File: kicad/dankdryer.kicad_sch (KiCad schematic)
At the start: 23 parts, among them J1 Barreljack, J4 heater, J6 Screw_Terminal_01x05, J7 5kg load cell, J8 motor, J9 Conn_01x04, U2 TPS62162DSG, U3 HT7550, U6 ESP32-C6-MINI-1U

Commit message: add 0.1uf capacitor to ADC input line closes #78
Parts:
- added C14: 0.1u, Capacitor_SMD:C_0805_2012Metric_Pad1.18x1.45mm_HandSolder, symbol Device:C
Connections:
- net GND: now also C14.1
- net Therm: now also C14.2
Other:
- note added: "ESP32 pins tolerate 20mA@3.3V. 412Ω+680Ω takes 5.3V to 3.369V and 5V to 3.178V, and limits current to 12.1mA. ESP32 ADC wants a 0.1uF filter capacitor "to improve accuracy"."
- note removed: "ESP32 pins tolerate 20mA@3.3V. 412Ω+680Ω takes 5.3V to 3.369V and 5V to 3.178V, and limits current to 12.1mA."
- moved on the sheet: R16, R18
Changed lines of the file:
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@@
 	)
 	(junction
+		(at 187.96 64.77)
+		(diameter 0)
+		(color 0 0 0 0)
+	)
+	(junction
 		(at 52.07 43.18)
 		(diameter 0)
@@
 	)
 	(junction
-		(at 71.12 147.32)
+		(at 66.04 147.32)
 		(diameter 0)
 		(color 0 0 0 0)
@@
 	)
 	(junction
+		(at 72.39 147.32)
+		(diameter 0)
+		(color 0 0 0 0)
+	)
+	(junction
 		(at 97.79 83.82)
 		(diameter 0)
@@
 	(wire
 		(pts
-			(xy 82.55 154.94) (xy 82.55 133.35)
+			(xy 82.55 137.16) (xy 82.55 133.35)
 		)
 		(stroke
@@
 	(wire
 		(pts
-			(xy 71.12 139.7) (xy 71.12 135.89)
+			(xy 66.04 139.7) (xy 66.04 135.89)
 		)
 		(stroke
@@
 	(wire
 		(pts
-			(xy 58.42 135.89) (xy 71.12 135.89)
+			(xy 58.42 135.89) (xy 66.04 135.89)
 		)
 		(stroke
@@
 	(wire
 		(pts
-			(xy 73.66 147.32) (xy 71.12 147.32)
+			(xy 74.93 147.32) (xy 72.39 147.32)
 		)
 		(stroke
@@
 	(wire
 		(pts
+			(xy 187.96 64.77) (xy 189.23 64.77)
+		)
+		(stroke
+			(width 0)
+			(type default)
+		)
+	)
+	(wire
+		(pts
 			(xy 132.08 185.42) (xy 127 185.42)
 		)
@@
 	(wire
 		(pts
+			(xy 72.39 147.32) (xy 66.04 147.32)
+		)
+		(stroke
+			(width 0)
+			(type default)
+		)
+	)
+	(wire
+		(pts
 			(xy 34.29 189.23) (xy 36.83 189.23)
 		)
@@
 	(wire
 		(pts
+			(xy 185.42 64.77) (xy 187.96 64.77)
+		)
+		(stroke
+			(width 0)
+			(type default)
+		)
+	)
+	(wire
+		(pts
 			(xy 219.71 85.09) (xy 223.52 85.09)
 		)
@@
 	(wire
 		(pts
+			(xy 187.96 68.58) (xy 187.96 64.77)
+		)
+		(stroke
+			(width 0)
+			(type default)
+		)
+	)
+	(wire
+		(pts
 			(xy 67.31 186.69) (xy 63.5 186.69)
 		)
@@
 		)
 	)
-	(text "ESP32 pins tolerate 20mA@3.3V.\n412Ω+680Ω takes 5.3V to 3.369V and 5V to 3.178V,\n and limits current to 12.1mA."
+	(text "ESP32 pins tolerate 20mA@3.3V.\n412Ω+680Ω takes 5.3V to 3.369V and 5V to 3.178V,\n and limits current to 12.1mA.\nESP32 ADC wants a 0.1uF filter capacitor \"to improve accuracy\"."
 		(exclude_from_sim no)
-		(at 21.336 164.084 0)
+		(at 21.082 163.576 0)
 		(effects
 			(font
@@
 	(hierarchical_label "Therm"
 		(shape bidirectional)
-		(at 189.23 64.77 180)
+		(at 185.42 64.77 180)
 		(fields_autoplaced yes)
 		(effects
@@
 	(hierarchical_label "Therm"
 		(shape input)
-		(at 73.66 147.32 0)
+		(at 74.93 147.32 0)
 		(fields_autoplaced yes)
 		(effects
@@
 	(symbol
 		(lib_id "Device:R")
-		(at 71.12 143.51 0)
+		(at 66.04 143.51 0)
 		(mirror x)
 		(unit 1)
@@
 		(fields_autoplaced yes)
 		(property "Reference" "R16"
-			(at 68.58 142.2399 0)
+			(at 63.5 142.2399 0)
 			(effects
 				(font
@@
 		)
 		(property "Value" "412"
-			(at 68.58 144.7799 0)
+			(at 63.5 144.7799 0)
 			(effects
 				(font
@@
 		)
 		(property "Footprint" "PCM_Resistor_SMD_AKL:R_0805_2012Metric_Pad1.15x1.40mm_HandSolder"
-			(at 69.342 143.51 90)
+			(at 64.262 143.51 90)
 			(effects
 				(font
@@
 		)
 		(property "Datasheet" "~"
-			(at 71.12 143.51 0)
+			(at 66.04 143.51 0)
 			(effects
 				(font
@@
 		)
 		(property "Description" "Resistor"
-			(at 71.12 143.51 0)
+			(at 66.04 143.51 0)
 			(effects
 				(font
@@
 	(symbol
 		(lib_id "Device:R")
-		(at 71.12 151.13 0)
+		(at 66.04 151.13 0)
 		(mirror x)
 		(unit 1)
@@
 		(fields_autoplaced yes)
 		(property "Reference" "R18"
-			(at 68.58 149.8599 0)
+			(at 63.5 149.8599 0)
 			(effects
 				(font
@@
 		)
 		(property "Value" "680"
-			(at 68.58 152.3999 0)
+			(at 63.5 152.3999 0)
 			(effects
 				(font
@@
 		)
 		(property "Footprint" "PCM_Resistor_SMD_AKL:R_0805_2012Metric_Pad1.15x1.40mm_HandSolder"
-			(at 69.342 151.13 90)
+			(at 64.262 151.13 90)
 			(effects
 				(font
@@
 		)
 		(property "Datasheet" "~"
-			(at 71.12 151.13 0)
+			(at 66.04 151.13 0)
 			(effects
 				(font
@@
 		)
 		(property "Description" "Resistor"
-			(at 71.12 151.13 0)
+			(at 66.04 151.13 0)
 			(effects
 				(font
@@
 	)
 	(symbol
+		(lib_id "Device:C")
+		(at 72.39 151.13 180)
+		(unit 1)
+		(exclude_from_sim no)
+		(in_bom yes)
+		(on_board yes)
+		(dnp no)
+		(property "Reference" "C14"
+			(at 77.724 150.114 0)
+			(effects
+				(font
+					(size 1.27 1.27)
+				)
+			)
+		)
+		(property "Value" "0.1u"
+			(at 77.47 152.4 0)
+			(effects
+				(font
+					(size 1.27 1.27)
+				)
+			)
+		)
+		(property "Footprint" "Capacitor_SMD:C_0805_2012Metric_Pad1.18x1.45mm_HandSolder"
+			(at 71.4248 147.32 0)
+			(effects
+				(font
+					(size 1.27 1.27)
+				)
+				(hide yes)
+			)
+		)
+		(property "Datasheet" "~"
+			(at 72.39 151.13 0)
+			(effects
+				(font
+					(size 1.27 1.27)
+				)
+				(hide yes)
+			)
+		)
+		(property "Description" "Unpolarized capacitor"
+			(at 72.39 151.13 0)
+			(effects
+				(font
+					(size 1.27 1.27)
+				)
+				(hide yes)
+			)
+		)
+		(pin "2"
+		)
+		(pin "1"
+		)
+		(instances
+			(project "dankdryer"
+				(path "/0e28ce9c-097a-4614-9b8c-9333a7b96611"
+					(reference "C14")
+					(unit 1)
+				)
+			)
+		)
+	)
+	(symbol
 		(lib_id "power:GND")
-		(at 82.55 154.94 0)
+		(at 82.55 137.16 0)
 		(mirror y)
 		(unit 1)
@@
 		(dnp no)
 		(property "Reference" "#PWR028"
-			(at 82.55 161.29 0)
+			(at 82.55 143.51 0)
 			(effects
 				(font
@@
 		)
 		(property "Value" "GND"
-			(at 82.55 160.02 0)
+			(at 82.55 142.24 0)
 			(effects
 				(font
@@
 		)
 		(property "Footprint" ""
-			(at 82.55 154.94 0)
+			(at 82.55 137.16 0)
 			(effects
 				(font
@@
 		)
 		(property "Datasheet" ""
-			(at 82.55 154.94 0)
+			(at 82.55 137.16 0)
 			(effects
 				(font
@@
 		)
 		(property "Description" "Power symbol creates a global label with name \"GND\" , ground"
-			(at 82.55 154.94 0)
+			(at 82.55 137.16 0)
 			(effects
 				(font
@@
 	(symbol
 		(lib_id "power:GND")
-		(at 71.12 154.94 0)
+		(at 66.04 154.94 0)
 		(unit 1)
 		(exclude_from_sim no)
@@
 		(fields_autoplaced yes)
 		(property "Reference" "#PWR034"
-			(at 71.12 161.29 0)
+			(at 66.04 161.29 0)
 			(effects
 				(font
@@
 		)
 		(property "Value" "GND"
-			(at 71.12 160.02 0)
+			(at 66.04 160.02 0)
 			(effects
 				(font
@@
 		)
 		(property "Footprint" ""
-			(at 71.12 154.94 0)
+			(at 66.04 154.94 0)
 			(effects
 				(font
@@
 		)
 		(property "Datasheet" ""
-			(at 71.12 154.94 0)
+			(at 66.04 154.94 0)
 			(effects
 				(font
@@
 		)
 		(property "Description" "Power symbol creates a global label with name \"GND\" , ground"
-			(at 71.12 154.94 0)
+			(at 66.04 154.94 0)
 			(effects
 				(font
@@
 					(unit 1)
 				)
+			)
+		)
+	)
+	(symbol
+		(lib_id "power:GND")
+		(at 72.39 154.94 0)
+		(unit 1)
+		(exclude_from_sim no)
+		(in_bom yes)
+		(on_board yes)
+		(dnp no)
+		(fields_autoplaced yes)
+		(property "Reference" "#PWR037"
+			(at 72.39 161.29 0)
+			(effects
+				(font
+					(size 1.27 1.27)
+				)
+				(hide yes)
+			)
+		)
+		(property "Value" "GND"
+			(at 72.39 160.02 0)
+			(effects
+				(font
+					(size 1.27 1.27)
+				)
+			)
+		)
+		(property "Footprint" ""
+			(at 72.39 154.94 0)
+			(effects
+				(font
+					(size 1.27 1.27)
+				)
+				(hide yes)
+			)
+		)
+		(property "Datasheet" ""
+			(at 72.39 154.94 0)
+			(effects
+				(font
+					(size 1.27 1.27)
+				)
+				(hide yes)
+			)
+		)
+		(property "Description" "Power symbol creates a global label with name \"GND\" , ground"
+			(at 72.39 154.94 0)
+			(effects
+				(font
+					(size 1.27 1.27)
+				)
+				(hide yes)
+			)
+		)
+		(pin "1"
+		)
+		(instances
+			(project "dankdryer"
+				(path "/0e28ce9c-097a-4614-9b8c-9333a7b96611"
+					(reference "#PWR037")
+					(unit 1)
+				)

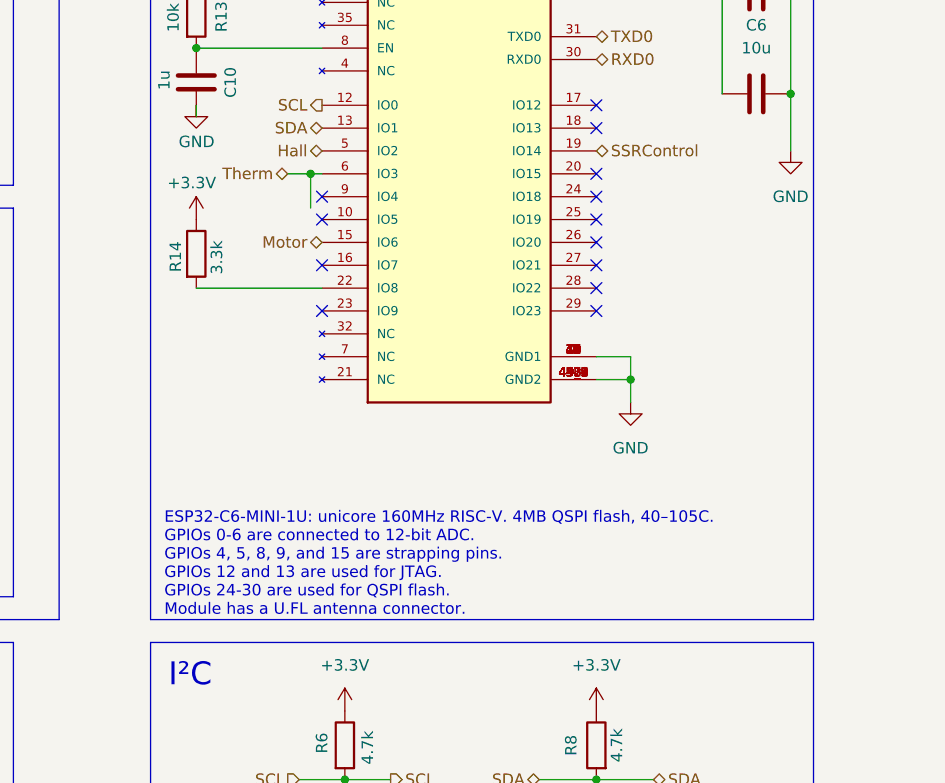
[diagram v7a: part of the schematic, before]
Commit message: move pullup from GPIO8 to GPIO9, ensuring SPI boot closes #79
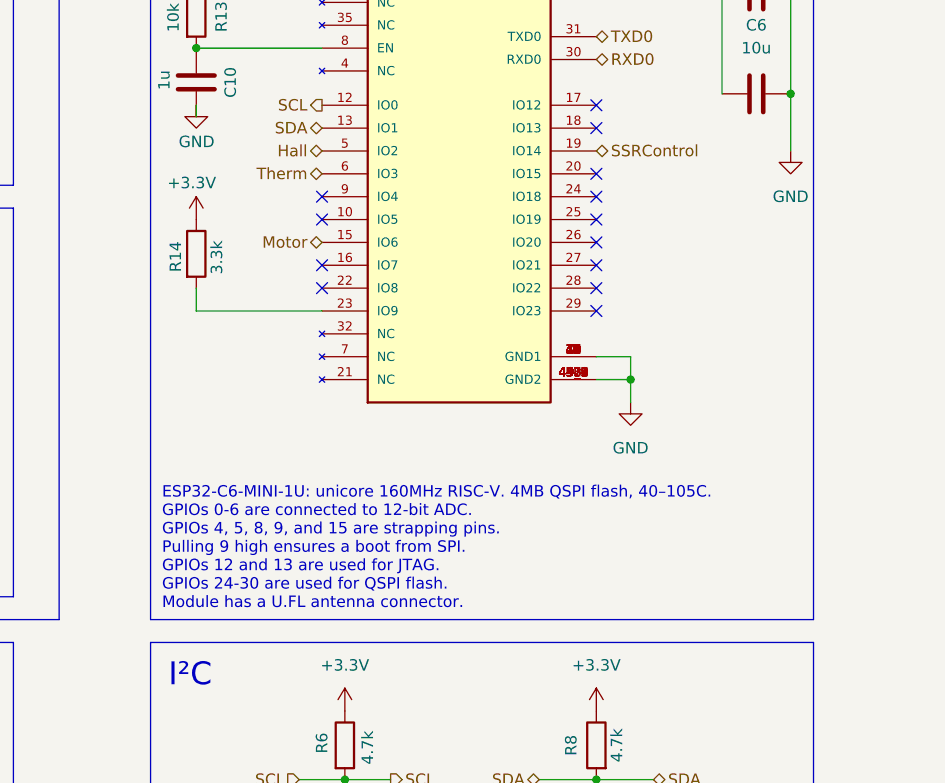
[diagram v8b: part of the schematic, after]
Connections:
- net at R14.2: now also U6.23 (IO9); no longer U6.22 (IO8)
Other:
- note added: "ESP32-C6-MINI-1U: unicore 160MHz RISC-V. 4MB QSPI flash, 40–105C. GPIOs 0-6 are connected to 12-bit ADC. GPIOs 4, 5, 8, 9, and 15 are strapping pins. Pulling 9 high ensures a boot from SPI. GPIOs 12 and 13 are used for JTAG. GPIOs 24-30 are used for QSPI flash. Module has a U.FL antenna connector."
- note removed: "ESP32-C6-MINI-1U: unicore 160MHz RISC-V. 4MB QSPI flash, 40–105C. GPIOs 0-6 are connected to 12-bit ADC. GPIOs 4, 5, 8, 9, and 15 are strapping pins. GPIOs 12 and 13 are used for JTAG. GPIOs 24-30 are used for QSPI flash. Module has a U.FL antenna connector."
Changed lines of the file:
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@@
-	)
-	(junction
-		(at 187.96 64.77)
-		(diameter 0)
-		(color 0 0 0 0)
 	)
 	(junction
@@
 	)
 	(no_connect
-		(at 189.23 80.01)
-	)
-	(no_connect
 		(at 219.71 74.93)
 	)
@@
 	)
 	(no_connect
+		(at 189.23 77.47)
+	)
+	(no_connect
 		(at 44.45 45.72)
 	)
@@
 	(wire
 		(pts
-			(xy 175.26 77.47) (xy 189.23 77.47)
-		)
-		(stroke
-			(width 0)
-			(type default)
-		)
-	)
-	(wire
-		(pts
 			(xy 58.42 135.89) (xy 66.04 135.89)
 		)
@@
 	(wire
 		(pts
-			(xy 187.96 64.77) (xy 189.23 64.77)
-		)
-		(stroke
-			(width 0)
-			(type default)
-		)
-	)
-	(wire
-		(pts
 			(xy 132.08 185.42) (xy 127 185.42)
 		)
@@
 	(wire
 		(pts
+			(xy 175.26 80.01) (xy 189.23 80.01)
+		)
+		(stroke
+			(width 0)
+			(type default)
+		)
+	)
+	(wire
+		(pts
 			(xy 82.55 125.73) (xy 82.55 130.81)
 		)
@@
 	(wire
 		(pts
-			(xy 185.42 64.77) (xy 187.96 64.77)
-		)
-		(stroke
-			(width 0)
-			(type default)
-		)
-	)
-	(wire
-		(pts
 			(xy 219.71 85.09) (xy 223.52 85.09)
 		)
@@
 	(wire
 		(pts
-			(xy 187.96 68.58) (xy 187.96 64.77)
-		)
-		(stroke
-			(width 0)
-			(type default)
-		)
-	)
-	(wire
-		(pts
 			(xy 67.31 186.69) (xy 63.5 186.69)
 		)
@@
 		(pts
 			(xy 219.71 132.08) (xy 226.06 132.08)
+		)
+		(stroke
+			(width 0)
+			(type default)
+		)
+	)
+	(wire
+		(pts
+			(xy 175.26 80.01) (xy 175.26 77.47)
 		)
 		(stroke
@@
 		)
 	)
-	(text "ESP32-C6-MINI-1U: unicore 160MHz RISC-V. 4MB QSPI flash, 40–105C.\nGPIOs 0-6 are connected to 12-bit ADC.\nGPIOs 4, 5, 8, 9, and 15 are strapping pins.\nGPIOs 12 and 13 are used for JTAG.\nGPIOs 24-30 are used for QSPI flash.\nModule has a U.FL antenna connector."
-		(exclude_from_sim no)
-		(at 171.704 108.204 0)
+	(text "ESP32-C6-MINI-1U: unicore 160MHz RISC-V. 4MB QSPI flash, 40–105C.\nGPIOs 0-6 are connected to 12-bit ADC.\nGPIOs 4, 5, 8, 9, and 15 are strapping pins.\nPulling 9 high ensures a boot from SPI.\nGPIOs 12 and 13 are used for JTAG.\nGPIOs 24-30 are used for QSPI flash.\nModule has a U.FL antenna connector."
+		(exclude_from_sim no)
+		(at 171.45 106.426 0)
 		(effects
 			(font
@@
 	(hierarchical_label "Therm"
 		(shape bidirectional)
-		(at 185.42 64.77 180)
+		(at 189.23 64.77 180)
 		(fields_autoplaced yes)
 		(effects
